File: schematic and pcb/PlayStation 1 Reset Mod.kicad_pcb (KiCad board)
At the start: 2 copper layers, 14.5 x 12 mm, 17 parts, among them U1 PIC16F18325-ISL

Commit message: updated schematic and PCB
fix issues #1, #2, #3, #5
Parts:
- removed R1: 10k, Resistor_SMD:R_1206_3216Metric_Pad1.42x1.75mm_HandSolder
- removed R2: 10k, Resistor_SMD:R_0805_2012Metric_Pad1.15x1.40mm_HandSolder
- C1, C2: value CP1_Small -> 0.1uF
- moved C2 0.17 mm to (132.3, 85.6)
- moved C1 0.10 mm to (132.3, 85.6)
- moved GND 0.06 mm to (139.2, 85.6)
- renumbered GND to VSS
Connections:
- net Net-(TP10-Pad1) renamed /RESET
- U1 pad 2: Net-(U1-Pad2) -> (no net)
- U1 pad 3: Net-(U1-Pad3) -> (no net)
- U1 pad 6: Net-(U1-Pad6) -> (no net)
- U1 pad 7: Net-(U1-Pad7) -> (no net)
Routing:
- net +3V3: track 19.9 -> 16.0 mm
- net /VPP\~MCLR: track 6.84 -> 5.69 mm

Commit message: specify jlc order number location
this fixes issue #8
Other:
- board text added: "JLCJLCJLCJLC"
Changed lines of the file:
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@@
   (general
     (thickness 1.6)
-    (drawings 8)
+    (drawings 9)
     (tracks 56)
     (zones 0)
@@
     )
   )
+  (gr_text JLCJLCJLCJLC (at 132.207 91.6178 90) (layer F.SilkS)
+    (effects (font (size 0.75 0.75) (thickness 0.15)))
+  )
   (gr_text "PS1 Reset Mod" (at 133.1354 85.1) (layer B.SilkS)

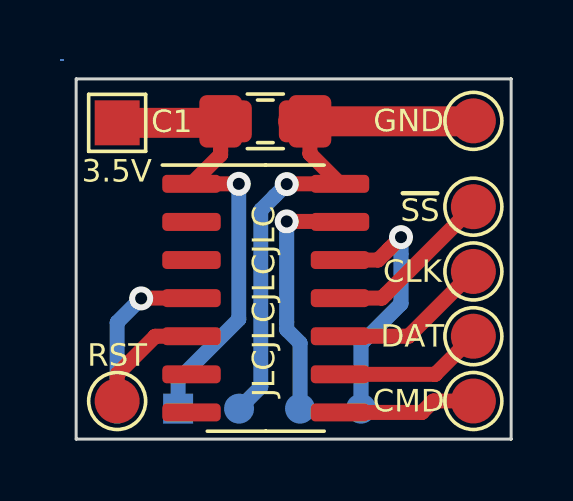
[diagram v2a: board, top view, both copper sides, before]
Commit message: added 0603 capacitor
I've added an extra 0603 capacitor footprint
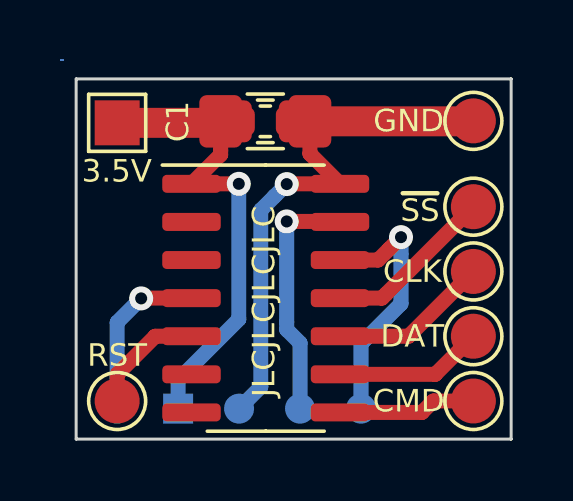
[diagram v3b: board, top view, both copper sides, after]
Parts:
- added C3: 0.1uF, Capacitor_SMD:C_0603_1608Metric_Pad1.05x0.95mm_HandSolder, F.Cu at (132.3, 85.6)
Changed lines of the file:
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@@
     (tracks 56)
     (zones 0)
-    (modules 15)
+    (modules 16)
     (nets 11)
   )
@@
   )
   (setup
-    (last_trace_width 0.5)
+    (last_trace_width 0.25)
     (user_trace_width 0.5)
     (user_trace_width 1)
@@
     (add_net "Net-(U1-Pad7)")
   )
+  (module Capacitor_SMD:C_0603_1608Metric_Pad1.05x0.95mm_HandSolder (layer F.Cu)
+    (at 132.2557 85.6142)
+    (descr "Capacitor SMD 0603 (1608 Metric), square (rectangular) end terminal, IPC_7351 nominal with elongated pad for handsoldering. (Body size source: http://www.tortai-tech.com/upload/download/2011102023233369053.pdf), generated with kicad-footprint-generator")
+    (tags "capacitor handsolder")
+    (attr smd)
+    (fp_text reference C3 (at 0 -1.43) (layer F.SilkS) hide
+      (effects (font (size 0.75 0.75) (thickness 0.15)))
+    )
+    (fp_text value 0.1uF (at 0 1.43) (layer F.Fab)
+      (effects (font (size 1 1) (thickness 0.15)))
+    )
+    (fp_text user %R (at 0 0) (layer F.Fab)
+      (effects (font (size 0.4 0.4) (thickness 0.06)))
+    )
+    (fp_line (start 1.65 0.73) (end -1.65 0.73) (layer F.CrtYd) (width 0.05))
+    (fp_line (start 1.65 -0.73) (end 1.65 0.73) (layer F.CrtYd) (width 0.05))
+    (fp_line (start -1.65 -0.73) (end 1.65 -0.73) (layer F.CrtYd) (width 0.05))
+    (fp_line (start -1.65 0.73) (end -1.65 -0.73) (layer F.CrtYd) (width 0.05))
+    (fp_line (start -0.171267 0.51) (end 0.171267 0.51) (layer F.SilkS) (width 0.12))
+    (fp_line (start -0.171267 -0.51) (end 0.171267 -0.51) (layer F.SilkS) (width 0.12))
+    (fp_line (start 0.8 0.4) (end -0.8 0.4) (layer F.Fab) (width 0.1))
+    (fp_line (start 0.8 -0.4) (end 0.8 0.4) (layer F.Fab) (width 0.1))
+    (fp_line (start -0.8 -0.4) (end 0.8 -0.4) (layer F.Fab) (width 0.1))
+    (fp_line (start -0.8 0.4) (end -0.8 -0.4) (layer F.Fab) (width 0.1))
+    (pad 2 smd roundrect (at 0.875 0) (size 1.05 0.95) (layers F.Cu F.Paste F.Mask) (roundrect_rratio 0.25)
+      (net 2 GND))
+    (pad 1 smd roundrect (at -0.875 0) (size 1.05 0.95) (layers F.Cu F.Paste F.Mask) (roundrect_rratio 0.25)
+      (net 1 +3V3))
+    (model ${KISYS3DMOD}/Capacitor_SMD.3dshapes/C_0603_1608Metric.wrl
+      (at (xyz 0 0 0))
+      (scale (xyz 1 1 1))
+      (rotate (xyz 0 0 0))
+    )
+  )
   (module TestPoint:TestPoint_Pad_D1.5mm (layer F.Cu)
     (at 139.1915 94.936)
@@
     (tags "capacitor handsolder")
     (attr smd)
-    (fp_text reference C1 (at -3.1221 0.0092 180) (layer F.SilkS)
-      (effects (font (size 0.75 0.75) (thickness 0.15)))
-    )
+    (fp_text reference C1 (at -2.9189 0.0092 270) (layer F.SilkS)
+      (effects (font (size 0.75 0.75) (thickness 0.15)))
+    )
